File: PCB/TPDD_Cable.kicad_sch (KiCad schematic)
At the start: 9 parts, among them J1 TPDD_RS-232C, P3 RX, P4 RTS, P5 CTS, P6 DSR, Q1 DTA114EKA, Q2 DTA114EKA, Q3 DTA114EKA

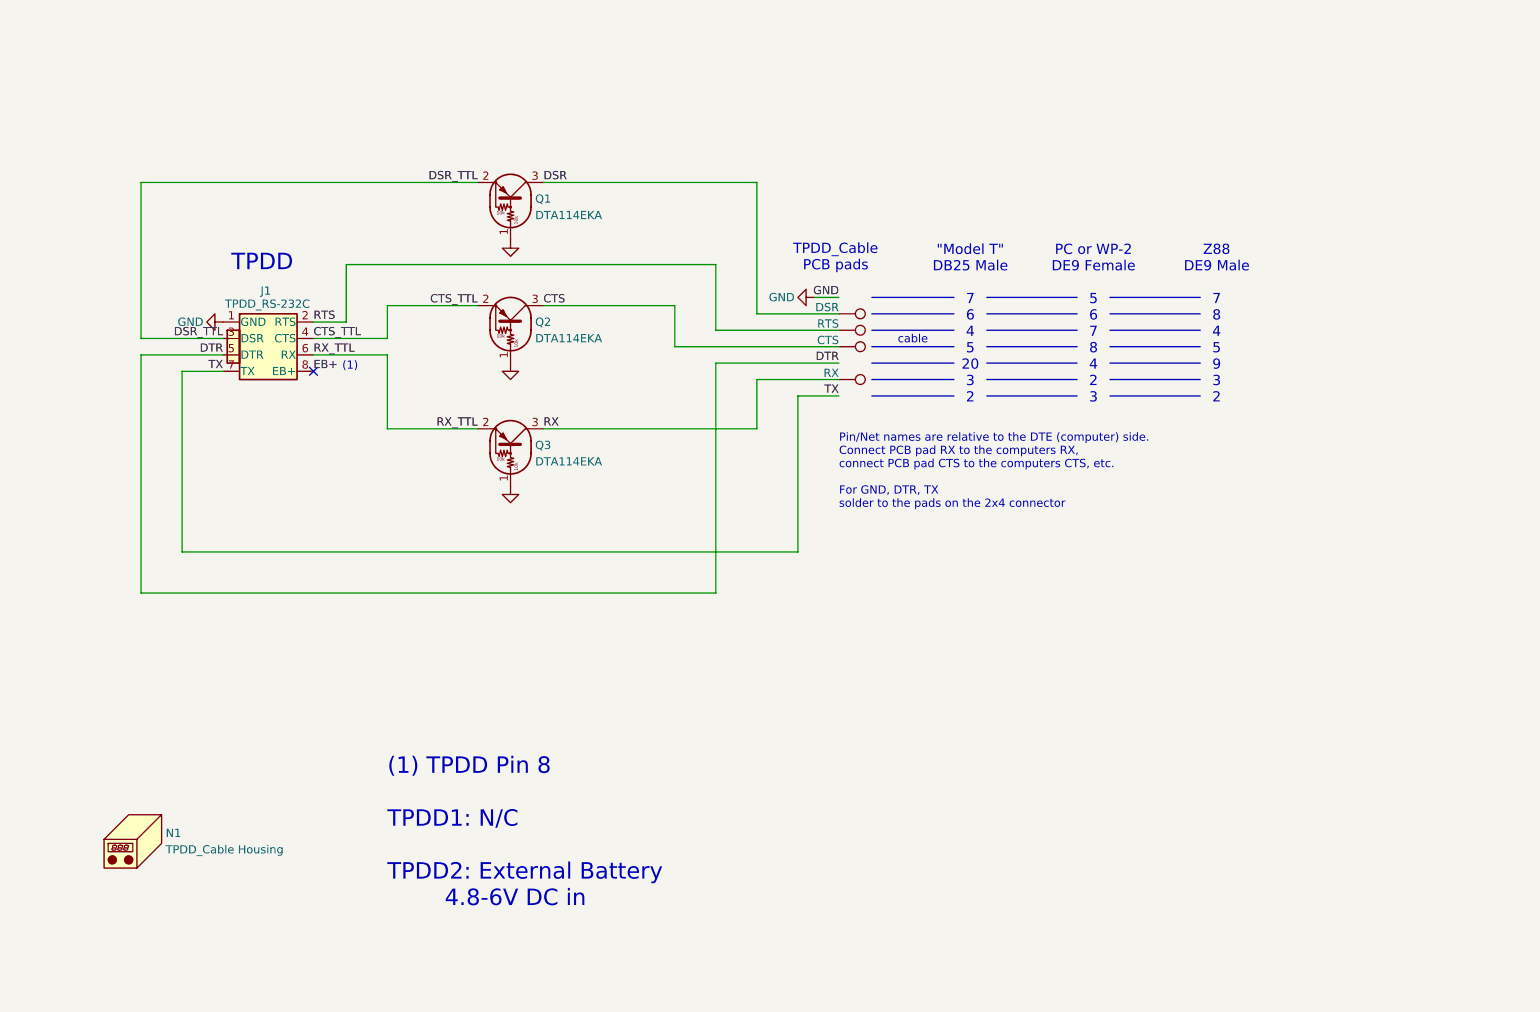
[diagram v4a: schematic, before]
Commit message: wire color charts
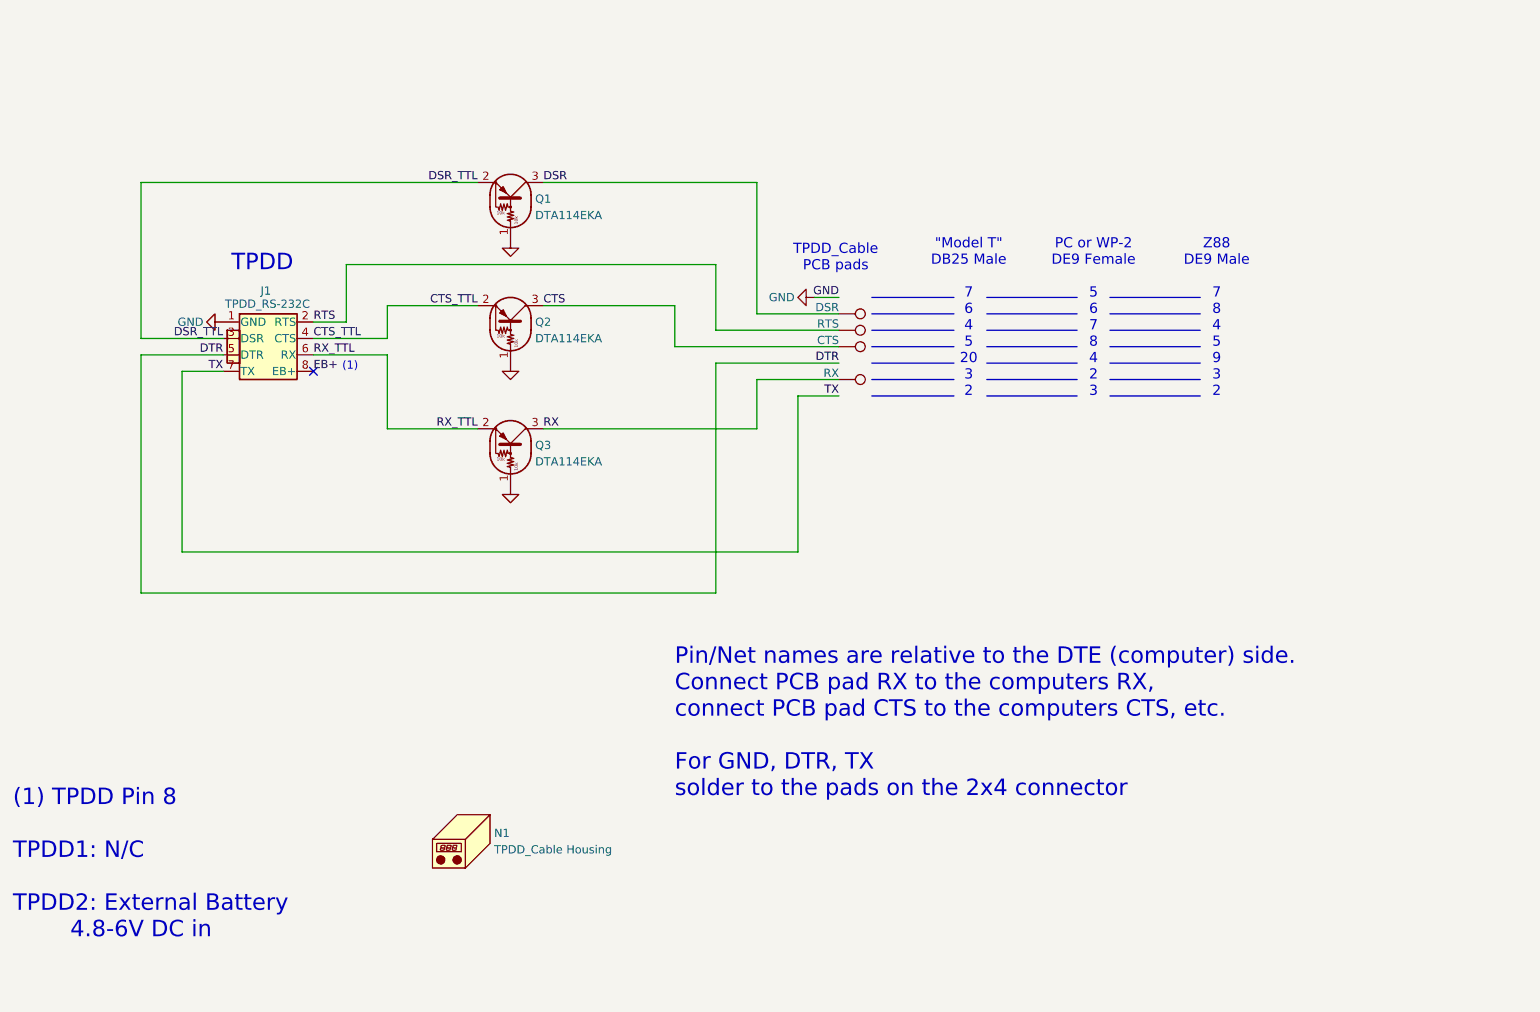
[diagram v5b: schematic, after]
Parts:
- J1: MPN (none) -> M20-7830442
- P3, P4, P5, P6: now left out of the parts list
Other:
- note removed: "cable"
- moved on the sheet: N1
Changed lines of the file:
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@@
 	(text "Z88\nDE9 Male\n\n7\n8\n4\n5\n9\n3\n2"
 		(exclude_from_sim no)
-		(at 229.87 73.152 0)
+		(at 229.87 72.136 0)
 		(effects
 			(font
@@
 	(text "(1) TPDD Pin 8\n\nTPDD1: N/C\n\nTPDD2: External Battery\n        4.8-6V DC in"
 		(exclude_from_sim no)
-		(at 101.6 152.4 0)
+		(at 43.688 157.226 0)
 		(effects
 			(font
@@
 		)
 	)
-	(text "cable"
-		(exclude_from_sim no)
-		(at 182.88 87.884 0)
-		(effects
-			(font
-				(size 1.27 1.27)
-			)
-		)
-	)
 	(text "Pin/Net names are relative to the DTE (computer) side.\nConnect PCB pad RX to the computers RX,\nconnect PCB pad CTS to the computers CTS, etc.\n\nFor GND, DTR, TX\nsolder to the pads on the 2x4 connector\n"
 		(exclude_from_sim no)
-		(at 171.45 102.362 0)
-		(effects
-			(font
-				(size 1.27 1.27)
+		(at 146.05 135.382 0)
+		(effects
+			(font
+				(size 2.54 2.54)
 			)
 			(justify left top)
@@
 	(text "PC or WP-2\nDE9 Female\n\n5\n6\n7\n8\n4\n2\n3"
 		(exclude_from_sim no)
-		(at 210.82 73.152 0)
+		(at 210.82 72.136 0)
 		(effects
 			(font
@@
 	(text "\"Model T\"\nDB25 Male\n\n7\n6\n4\n5\n20\n3\n2"
 		(exclude_from_sim no)
-		(at 191.77 73.152 0)
+		(at 191.516 72.136 0)
 		(effects
 			(font
@@
 	(symbol
 		(lib_id "000_LOCAL:Housing")
-		(at 63.5 165.1 0)
+		(at 114.3 165.1 0)
 		(unit 1)
 		(exclude_from_sim yes)
@@
 		(fields_autoplaced yes)
 		(property "Reference" "N1"
-			(at 67.31 164.1474 0)
+			(at 118.11 164.1474 0)
 			(effects
 				(font
@@
 		)
 		(property "Value" "TPDD_Cable Housing"
-			(at 67.31 166.6874 0)
+			(at 118.11 166.6874 0)
 			(effects
 				(font
@@
 		)
 		(property "Footprint" "000_LOCAL:TPDD_Cable_Housing"
-			(at 64.77 163.83 0)
+			(at 115.57 163.83 0)
 			(effects
 				(font
@@
 		)
 		(property "Datasheet" "~"
-			(at 64.77 163.83 0)
+			(at 115.57 163.83 0)
 			(effects
 				(font
@@
 		)
 		(property "Description" "Housing"
-			(at 63.5 165.1 0)
+			(at 114.3 165.1 0)
 			(effects
 				(font
@@
 		(unit 1)
 		(exclude_from_sim no)
-		(in_bom yes)
+		(in_bom no)
 		(on_board yes)
 		(dnp no)
@@
 			)
 		)
+		(property "MPN" "M20-7830442"
+			(at 82.55 87.63 0)
+			(effects
+				(font
+					(size 1.27 1.27)
+				)
+				(hide yes)
+			)
+		)
 		(pin "5"
 		)
@@
 		)
 		(instances
+			(project ""
+				(path "/0d433bab-64ac-46dd-8906-cd1b476f2235"
+					(reference "J1")
+					(unit 1)
+				)
+			)
 			(project ""
 				(path "/8c978a26-63bd-42ef-84db-2107e27041da/837a9c0d-b7a0-4105-85d5-9798010a27dd"
@@
 		(unit 1)
 		(exclude_from_sim no)
-		(in_bom yes)
+		(in_bom no)
 		(on_board yes)
 		(dnp no)
@@
 		(unit 1)
 		(exclude_from_sim no)
-		(in_bom yes)
+		(in_bom no)
 		(on_board yes)
 		(dnp no)
@@
 		(unit 1)
 		(exclude_from_sim no)
-		(in_bom yes)
-		(on_board yes)
-		(dnp no)
+		(in_bom no)
+		(on_board yes)
+		(dnp no)

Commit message: fab bom & pics
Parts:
- N1: now left out of the parts list
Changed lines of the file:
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@@
 		(unit 1)
 		(exclude_from_sim yes)
-		(in_bom yes)
+		(in_bom no)
 		(on_board yes)
 		(dnp no)
@@
 		)
 		(instances
+			(project ""
+				(path "/0d433bab-64ac-46dd-8906-cd1b476f2235"
+					(reference "N1")
+					(unit 1)
+				)
+			)
 			(project "TPDD_Cable_2"
 				(path "/8c978a26-63bd-42ef-84db-2107e27041da/837a9c0d-b7a0-4105-85d5-9798010a27dd"
@@
 			)
 		)
-		(property "Datasheet" "~"
+		(property "Datasheet" "datasheets/M20-783.pdf"
 			(at 85.09 87.63 0)
 			(effects
